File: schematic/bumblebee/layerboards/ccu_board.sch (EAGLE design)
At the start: 11 parts

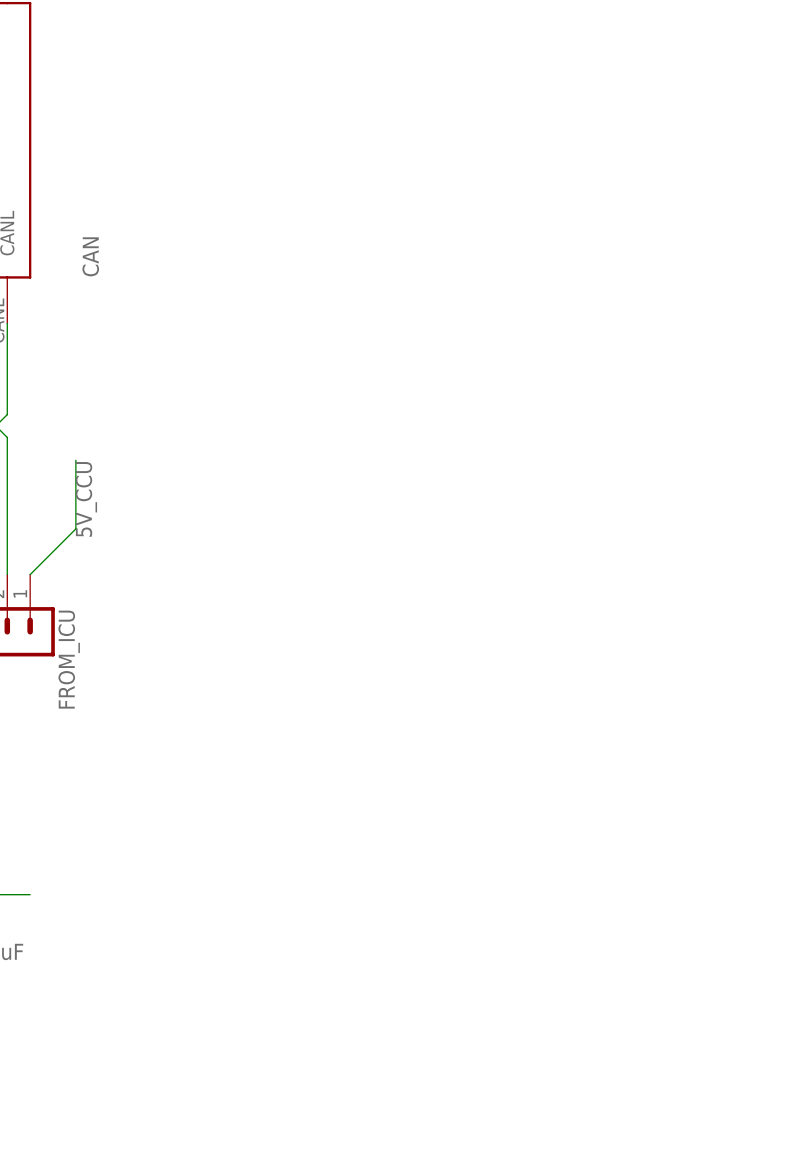
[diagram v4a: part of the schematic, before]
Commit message: Добавлена плата АЦП на CCU Сделана и разведена внешняя плата Кое-что сделал в либе
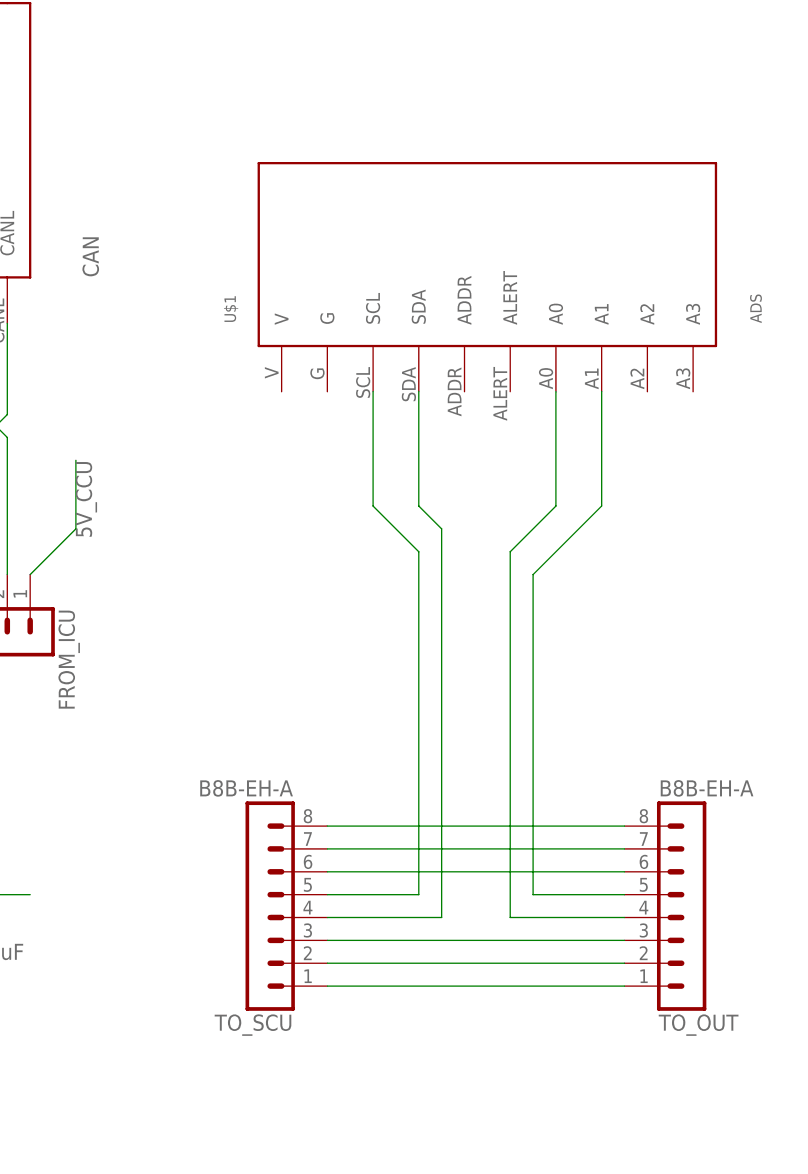
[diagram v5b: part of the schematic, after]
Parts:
- added TO_OUT, TO_SCU: B8B-EH-A, con-jst-eh:B8B-EH-A
- added U$1: ADS, bluepill:ADS
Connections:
- new net N$1: TO_OUT.8, TO_SCU.8
- new net N$10: TO_SCU.4, U$1.SDA
- new net N$12: TO_OUT.5, U$1.A1
- new net N$13: TO_OUT.4, U$1.A0
- new net N$2: TO_OUT.7, TO_SCU.7
- new net N$3: TO_OUT.6, TO_SCU.6
- new net N$4: TO_OUT.3, TO_SCU.3
- new net N$5: TO_OUT.2, TO_SCU.2
- new net N$7: TO_OUT.1, TO_SCU.1
- new net N$9: TO_SCU.5, U$1.SCL
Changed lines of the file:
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@@
 <?xml version="1.0" encoding="utf-8"?>
 <!DOCTYPE eagle SYSTEM "eagle.dtd">
-<eagle version="9.3.2">
+<eagle version="9.3.0">
 <drawing>
 <settings>
@@
 <part name="CAM_UP" library="con-jst-eh" deviceset="B4B-EH-A" device=""/>
 <part name="CAM_DOWN" library="con-jst-eh" deviceset="B4B-EH-A" device=""/>
+<part name="TO_SCU" library="con-jst-eh" deviceset="B8B-EH-A" device=""/>
+<part name="TO_OUT" library="con-jst-eh" deviceset="B8B-EH-A" device=""/>
+<part name="U$1" library="bluepill" deviceset="ADS" device=""/>
 </parts>
 <sheets>
@@
 <attribute name="NAME" x="41.275" y="-49.53" size="1.778" layer="95" rot="R270"/>
 <attribute name="VALUE" x="25.4" y="-49.53" size="1.778" layer="95" rot="R270"/>
+</instance>
+<instance part="TO_SCU" gate="G$1" x="147.32" y="-76.2" smashed="yes" rot="R180">
+<attribute name="NAME" x="148.59" y="-89.535" size="1.778" layer="95" rot="R180"/>
+<attribute name="VALUE" x="148.59" y="-63.5" size="1.778" layer="95" rot="R180"/>
+</instance>
+<instance part="TO_OUT" gate="G$1" x="190.5" y="-76.2" smashed="yes" rot="MR180">
+<attribute name="NAME" x="189.23" y="-89.535" size="1.778" layer="95" rot="MR180"/>
+<attribute name="VALUE" x="189.23" y="-63.5" size="1.778" layer="95" rot="MR180"/>
+</instance>
+<instance part="U$1" gate="G$1" x="170.18" y="-5.08" smashed="yes" rot="R90">
+<attribute name="NAME" x="142.24" y="-12.7" size="1.27" layer="95" rot="R90"/>
+<attribute name="VALUE" x="200.66" y="-12.7" size="1.27" layer="96" rot="R90"/>
 </instance>
 </instances>
@@
 </segment>
 </net>
+<net name="N$1" class="0">
+<segment>
+<pinref part="TO_SCU" gate="G$1" pin="8"/>
+<pinref part="TO_OUT" gate="G$1" pin="8"/>
+<wire x1="152.4" y1="-68.58" x2="185.42" y2="-68.58" width="0.1524" layer="91"/>
+</segment>
+</net>
+<net name="N$2" class="0">
+<segment>
+<pinref part="TO_SCU" gate="G$1" pin="7"/>
+<pinref part="TO_OUT" gate="G$1" pin="7"/>
+<wire x1="152.4" y1="-71.12" x2="185.42" y2="-71.12" width="0.1524" layer="91"/>
+</segment>
+</net>
+<net name="N$3" class="0">
+<segment>
+<pinref part="TO_SCU" gate="G$1" pin="6"/>
+<pinref part="TO_OUT" gate="G$1" pin="6"/>
+<wire x1="152.4" y1="-73.66" x2="185.42" y2="-73.66" width="0.1524" layer="91"/>
+</segment>
+</net>
+<net name="N$4" class="0">
+<segment>
+<pinref part="TO_SCU" gate="G$1" pin="3"/>
+<pinref part="TO_OUT" gate="G$1" pin="3"/>
+<wire x1="152.4" y1="-81.28" x2="185.42" y2="-81.28" width="0.1524" layer="91"/>
+</segment>
+</net>
+<net name="N$5" class="0">
+<segment>
+<pinref part="TO_SCU" gate="G$1" pin="2"/>
+<pinref part="TO_OUT" gate="G$1" pin="2"/>
+<wire x1="152.4" y1="-83.82" x2="185.42" y2="-83.82" width="0.1524" layer="91"/>
+</segment>
+</net>
+<net name="N$7" class="0">
+<segment>
+<pinref part="TO_SCU" gate="G$1" pin="1"/>
+<pinref part="TO_OUT" gate="G$1" pin="1"/>
+<wire x1="152.4" y1="-86.36" x2="185.42" y2="-86.36" width="0.1524" layer="91"/>
+</segment>
+</net>
+<net name="N$9" class="0">
+<segment>
+<pinref part="TO_SCU" gate="G$1" pin="5"/>
+<wire x1="152.4" y1="-76.2" x2="162.56" y2="-76.2" width="0.1524" layer="91"/>
+<wire x1="162.56" y1="-76.2" x2="162.56" y2="-38.1" width="0.1524" layer="91"/>
+<wire x1="162.56" y1="-38.1" x2="157.48" y2="-33.02" width="0.1524" layer="91"/>
+<pinref part="U$1" gate="G$1" pin="SCL"/>
+<wire x1="157.48" y1="-33.02" x2="157.48" y2="-20.32" width="0.1524" layer="91"/>
+</segment>
+</net>
+<net name="N$10" class="0">
+<segment>
+<pinref part="TO_SCU" gate="G$1" pin="4"/>
+<wire x1="152.4" y1="-78.74" x2="165.1" y2="-78.74" width="0.1524" layer="91"/>
+<wire x1="165.1" y1="-78.74" x2="165.1" y2="-35.56" width="0.1524" layer="91"/>
+<wire x1="165.1" y1="-35.56" x2="162.56" y2="-33.02" width="0.1524" layer="91"/>
+<pinref part="U$1" gate="G$1" pin="SDA"/>
+<wire x1="162.56" y1="-33.02" x2="162.56" y2="-20.32" width="0.1524" layer="91"/>
+</segment>
+</net>
+<net name="N$12" class="0">
+<segment>
+<pinref part="TO_OUT" gate="G$1" pin="5"/>
+<wire x1="185.42" y1="-76.2" x2="175.26" y2="-76.2" width="0.1524" layer="91"/>
+<wire x1="175.26" y1="-76.2" x2="175.26" y2="-40.64" width="0.1524" layer="91"/>
+<wire x1="175.26" y1="-40.64" x2="182.88" y2="-33.02" width="0.1524" layer="91"/>
+<pinref part="U$1" gate="G$1" pin="A1"/>
+<wire x1="182.88" y1="-33.02" x2="182.88" y2="-20.32" width="0.1524" layer="91"/>
+</segment>
+</net>
+<net name="N$13" class="0">
+<segment>
+<pinref part="TO_OUT" gate="G$1" pin="4"/>
+<wire x1="185.42" y1="-78.74" x2="172.72" y2="-78.74" width="0.1524" layer="91"/>
+<wire x1="172.72" y1="-78.74" x2="172.72" y2="-38.1" width="0.1524" layer="91"/>
+<wire x1="172.72" y1="-38.1" x2="177.8" y2="-33.02" width="0.1524" layer="91"/>
+<pinref part="U$1" gate="G$1" pin="A0"/>
+<wire x1="177.8" y1="-33.02" x2="177.8" y2="-20.32" width="0.1524" layer="91"/>
+</segment>
+</net>
